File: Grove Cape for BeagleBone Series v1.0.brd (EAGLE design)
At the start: 71 x 55.2 mm, 74 parts, among them J1 SMD Grove-90D, J10 12p 0.5mm bottom contact, J11 12p 0.5mm bottom contact, J2 SMD Grove-90D, J3 SMD Grove, J5 SMD Grove-90D, J6 SMD Grove-90D, J7 SMD Grove, Q1 BAT54S, Q10 BAT54S, Q2 BAT54S, Q3 BAT54S, Q4 BAT54S, Q7 BAT54S, Q8 BAT54S, Q9 BAT54S, U1 EEPROM-I2CSMD

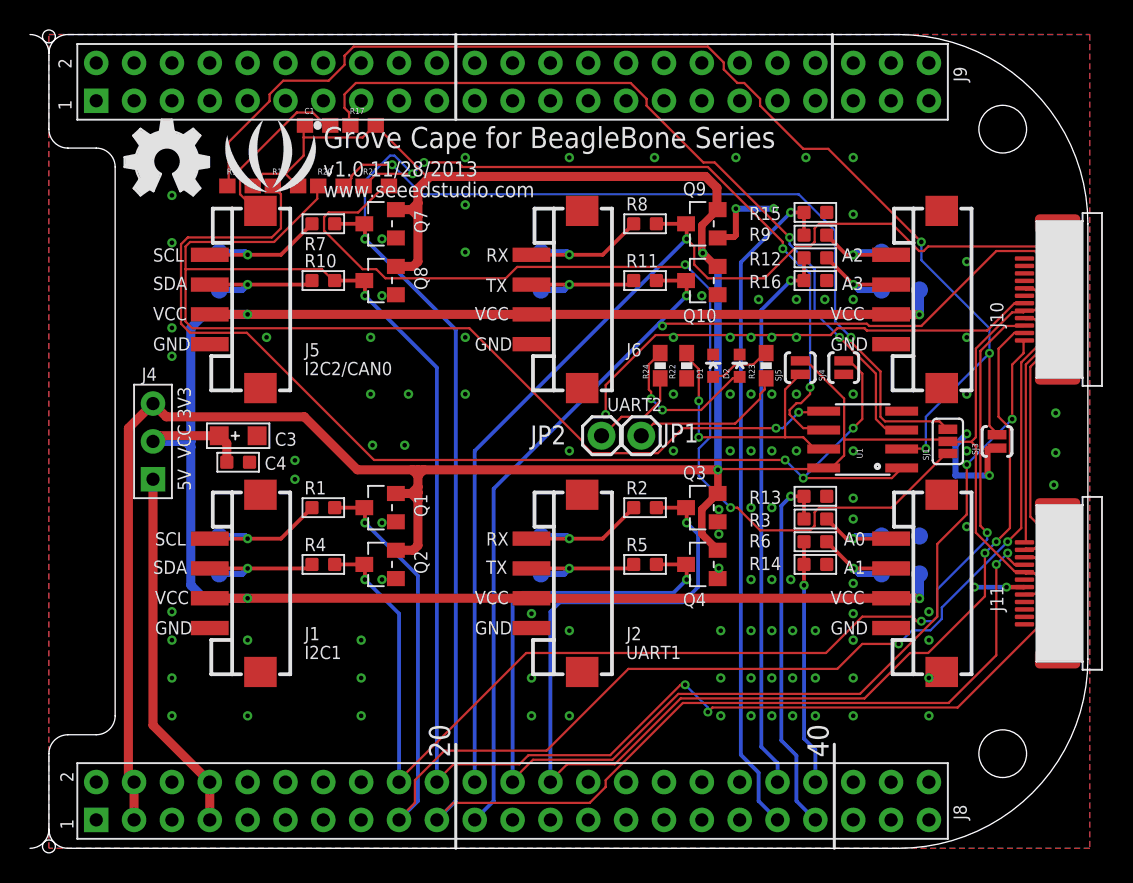
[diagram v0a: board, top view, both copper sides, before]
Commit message: Fixed component position and silk Screen
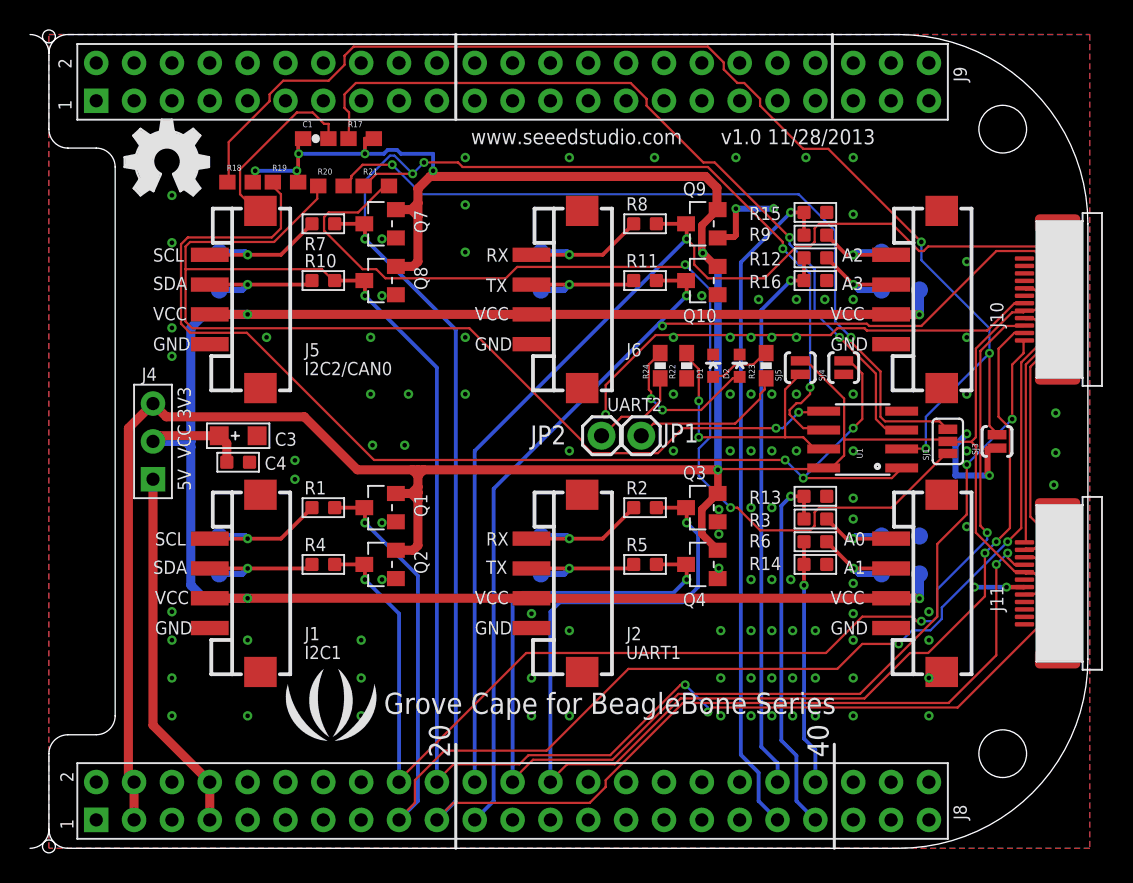
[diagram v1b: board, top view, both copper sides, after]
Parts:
- moved U$29 37.1 mm to (19.1, 8.89)
- moved C1 0.90 mm to (18.0, 47.6)
- moved R17 0.90 mm to (21.1, 47.6)
- moved R18 0.25 mm to (13.0, 44.7)
- moved R19 0.25 mm to (16.0, 44.7)
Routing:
- net 3V3: track 206.7 -> 209.0 mm, vias 2 -> 7
- net N$1: track 53.6 -> 54.5 mm
- net GND: track 61.5 -> 62.4 mm
